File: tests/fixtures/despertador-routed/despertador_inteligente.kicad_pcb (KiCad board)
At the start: 2 copper layers, 55 x 55 mm, 24 parts, among them J1 Conector ICSP, J2 CSE, U1 ATtiny85-20S, U2 MPU-6050, U3 MAX30102, U4 RFM69CW

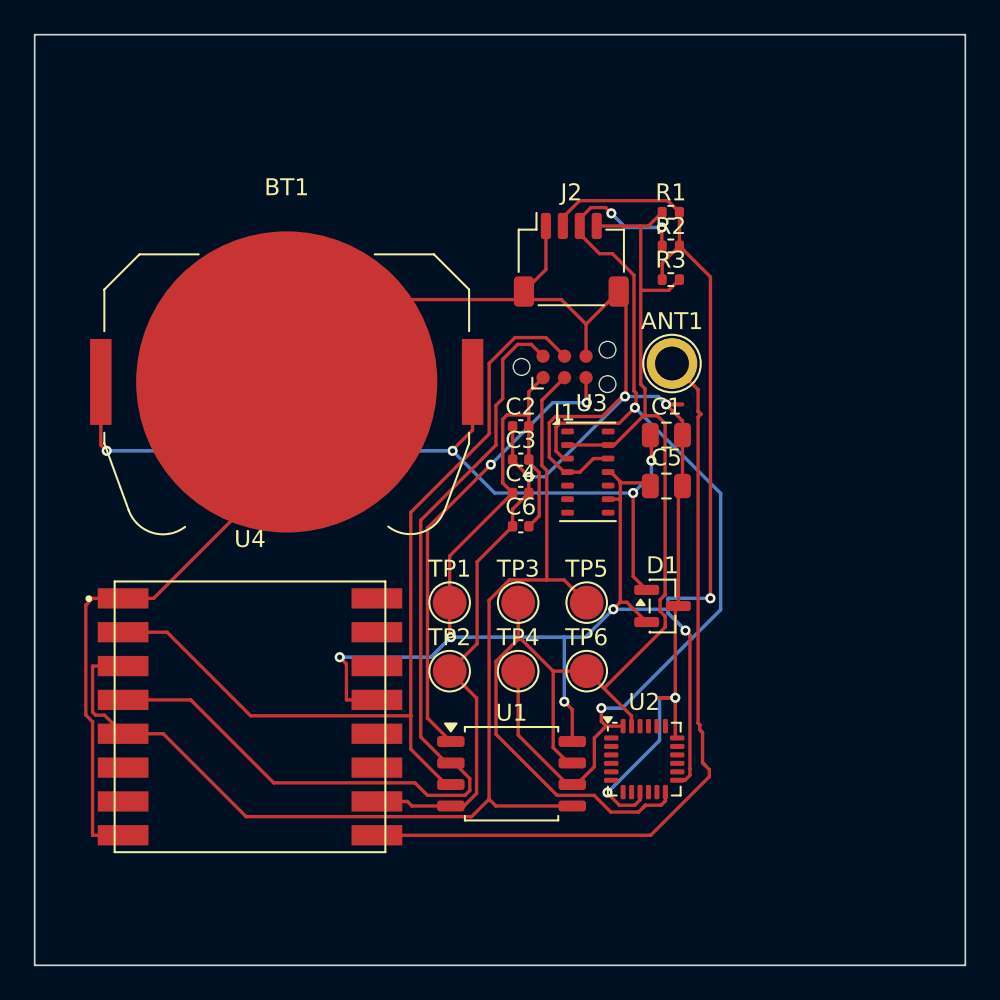
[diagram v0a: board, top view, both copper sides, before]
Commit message: post-D3 contecto actualizado CONTEXT-V3.md y frecciones D3 en ocs/dogfooding/dogfood3-fricciones.md
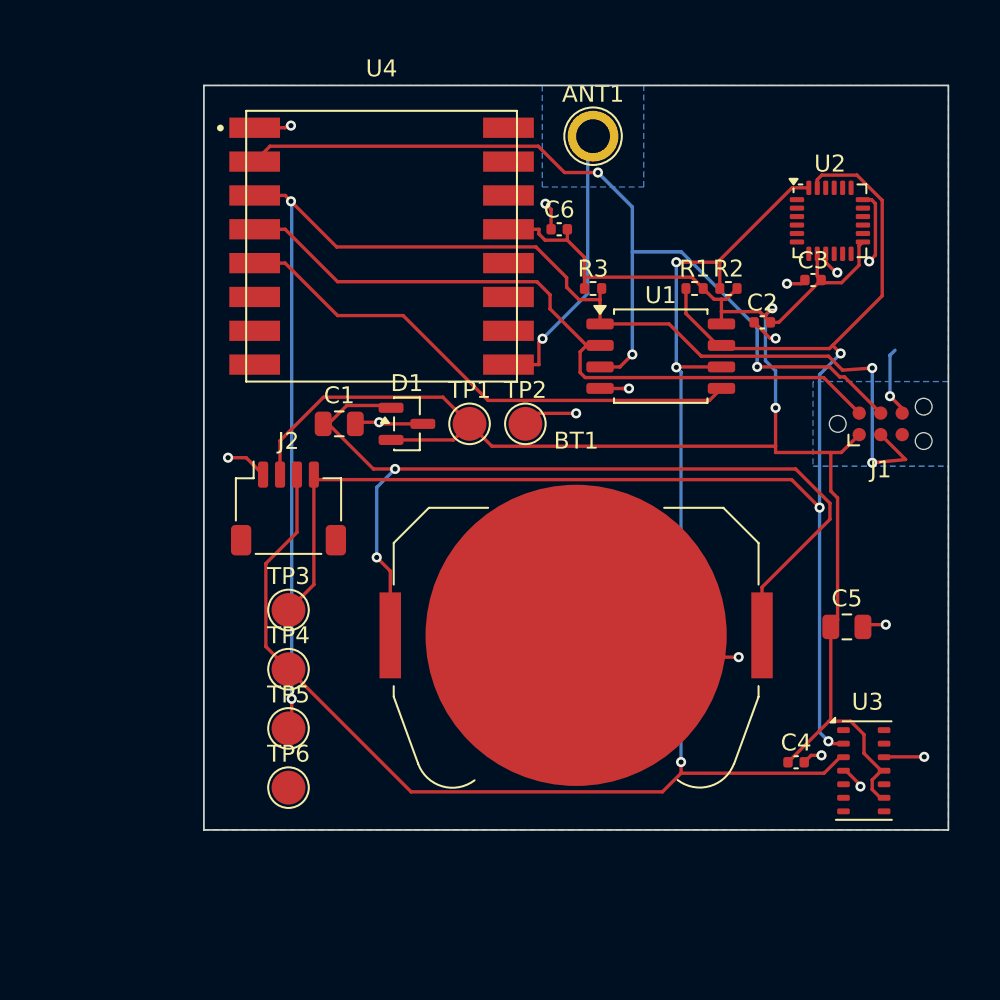
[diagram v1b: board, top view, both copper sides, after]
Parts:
- moved U2 33.7 mm to (187.0, 36.0)
- moved U4 28.9 mm to (160.5, 37.5)
- moved U1 26.2 mm to (177.0, 44.0)
- moved U3 24.0 mm to (189.0, 68.5)
- moved C4 22.8 mm to (185.0, 68.0)
- moved BT1 22.7 mm to (172.0, 60.5)
- moved J2 22.3 mm to (155.0, 53.0)
- moved C3 20.3 mm to (186.0, 39.5)
- moved C1 19.3 mm to (158.0, 48.0)
- moved TP5 19.1 mm to (155.0, 66.0)
- moved J1 19.0 mm to (190.0, 48.0)
- moved TP6 18.9 mm to (155.0, 69.5)
- moved D1 18.5 mm to (162.0, 48.0)
- moved C6 17.7 mm to (171.0, 36.5)
- moved C2 15.5 mm to (183.0, 42.0)
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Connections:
- J1 pad 5: /RESET -> unconnected-(J1-Pad5)
- J2 pad 4: /INT_SENS -> /SCL
- J2 pad MP: GND -> (no net)
- R1 pad 1: /INT_SENS -> /SCL
- R3 pad 2: /INT_SENS -> /MOSI
- TP3 pad 1: /INT_SENS -> /SCL
- U1 pad 1: /RESET -> /MOSI
- U1 pad 5: /MOSI -> /NSS
- U1 pad 7: /INT_SENS -> /SCL
- U2 pad 12: /INT_SENS -> unconnected-(U2-INT-Pad12)
- U2 pad 23: /INT_SENS -> /SCL
- U3 pad 13: /INT_SENS -> unconnected-(U3-~{INT}-Pad13)
- U3 pad 2: /INT_SENS -> /SCL
- U4 pad 10: GND -> (no net)
- U4 pad 5: /MOSI -> /NSS
- U4 pad 8: GND -> (no net)
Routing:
- net GND: track 161.5 -> 46.6 mm, vias 5 -> 16
- net /SCL: track 0.00 -> 90.4 mm, vias 0 -> 3
- net /INT_SENS: track 78.6 -> 0.00 mm
- net /NSS: track 0.00 -> 31.2 mm
- net Net-(ANT1-A): track 47.4 -> 16.6 mm, vias 0 -> 1
- net /SDA: track 65.4 -> 93.7 mm, vias 4 -> 3
- net /RESET: track 27.2 -> 0.00 mm, vias 2 -> 0
- net /MOSI: track 67.2 -> 83.6 mm, vias 0 -> 4
- net /SCK: track 54.9 -> 43.0 mm
- net +3V3: track 119.1 -> 112.7 mm, vias 6 -> 2
- net Net-(BT1-+): track 51.8 -> 56.2 mm, vias 4 -> 2
- net /MISO: track 52.5 -> 55.1 mm, vias 0 -> 3
- added copper zone on B.Cu, net GND
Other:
- board size 55 x 55 mm -> 44 x 44 mm
